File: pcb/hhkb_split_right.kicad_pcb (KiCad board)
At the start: 4 copper layers, 173.7 x 97.4 mm, 84 parts, among them SW1 6, SW10 Y, SW11 U, SW12 I, SW13 O, SW14 P, SW15 [, SW16 ], SW17 Del, SW18 H, SW19 J, SW2 7, SW20 K, SW21 L, SW22 ;, SW23 ', SW24 Enter, SW25 N, SW26 M, SW27 ,, SW28 ., SW29 /, SW3 8, SW30 Shift, SW31 Fn, SW32 R-Space, SW33 Meta, SW34 Alt, SW4 9, SW5 0, SW6 -, SW7 =, SW8 \, SW9 `, U1 74HC595, U2 74HC595

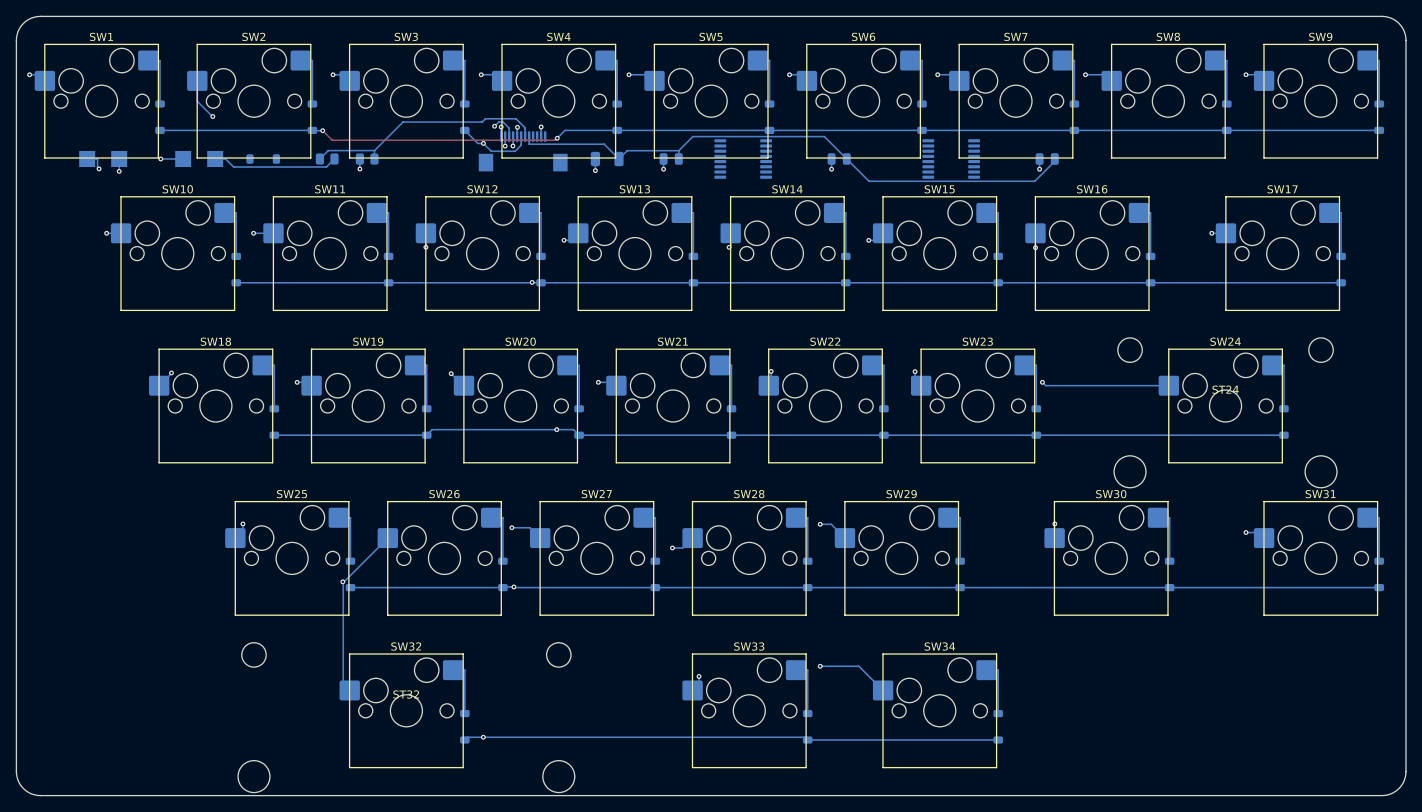
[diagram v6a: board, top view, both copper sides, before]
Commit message: マトリクスのダイオードを SD103AW にした（打ち止めが保証値で決まる）
1N4148W は **1mA 未満の Vf 最大値を規定していない**。行に届くのは
（レール − Vf）で nRF52840 の VIH は 0.7×レール、つまり レール ≧ Vf/0.3。
1mA の最大 0.715V で詰めるとレール 2.55V（1.48V/本）が必要になり、
**打ち止めが 1.12〜1.48V/本 の間で不定だった。電池が減るとキーが
反応しなくなる。**

SD103AW（C130875）は **VF ≦ 0.37V @ 20mA を保証**している。実使用は
100µA でそれよりはるかに小さい。必要なレールは 1.40V で、マイコンの
1.80V の内側。**打ち止めはマイコン律速の 1.10V/本 に戻った。実測不要。**

  逆漏れ 5µA @ 30V（実使用 2V ではさらに小さい）。プルダウン 13kΩ に対し
  誤検出には 20 個以上の同時押しが要る
  フットプリントは同じ SOD-123。**基板は変わらない**（Value は B.Fab のみ）
  単価 $0.0116 で 1N4148W とほぼ同じ。Basic → Extended で +$3

3 基板とも DRC 0 / 未配線 0。検査 292 件。部品 8 種すべて在庫を再確認した。
C4 からダイオードの実測手順を削り、provisional-values から
MATRIX_DIODE_VF を外した（保証値になったため）。

Co-Authored-By: Claude Opus 5 (1M context) <noreply@anthropic.com>
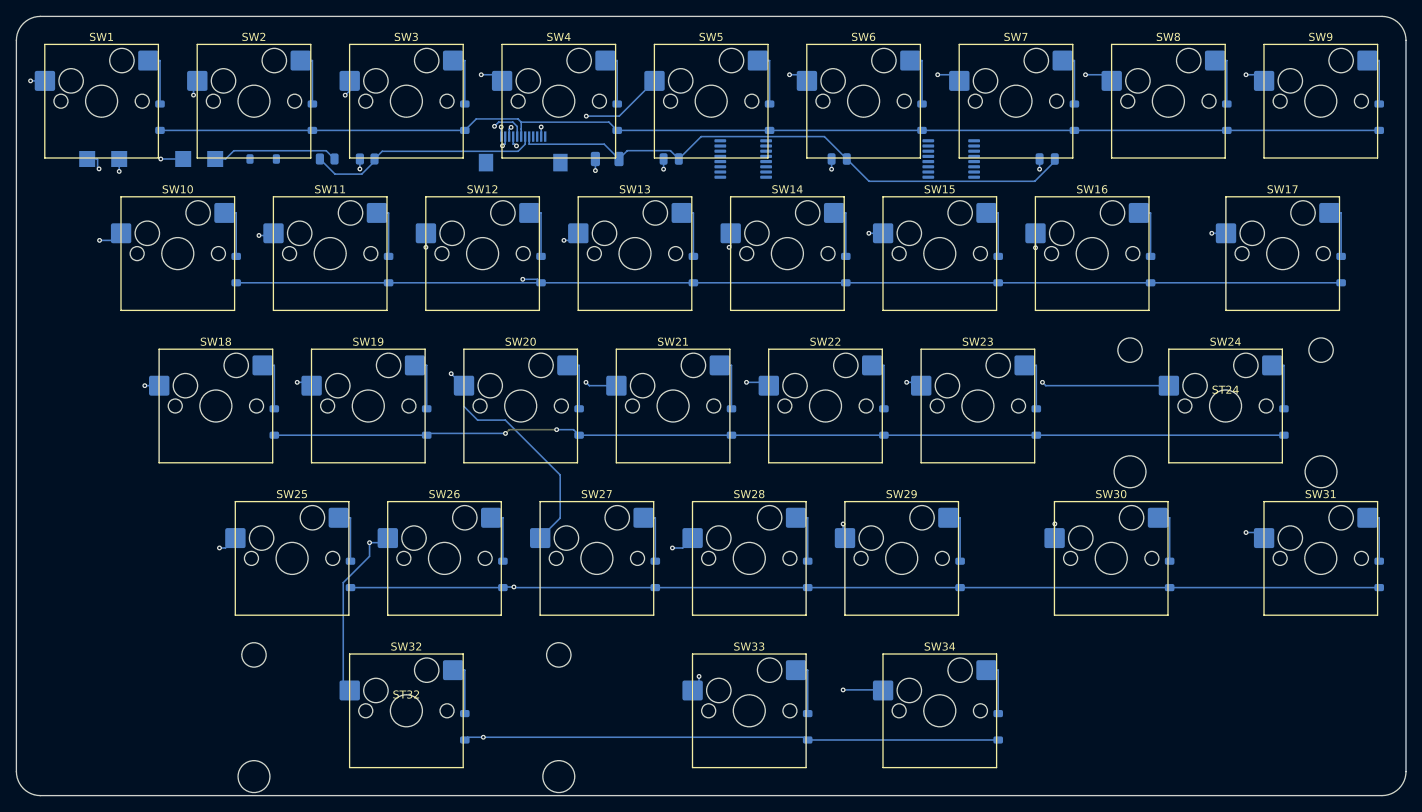
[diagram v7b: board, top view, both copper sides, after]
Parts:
- D1, D10, D11, D12, D13, D14, D15, D16, D17, D18, D19, D2, D20, D21, D22, D23, D24, D25, D26, D27, D28, D29, D3, D30, D31, D32, D33, D34, D4, D5, D6, D7, D8, D9: value 1N4148W -> SD103AW
- U1, U2: value 74HC595 -> 74LVC595
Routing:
- net ROW0: track 163.3 -> 155.4 mm, vias 3 -> 0
- net ROW1: track 160.1 -> 167.1 mm
- net COL2: track 99.1 -> 92.7 mm
- net COL1: track 74.8 -> 78.0 mm
- net VBATT_SENSE: track 30.3 -> 29.1 mm
- net COL4: track 98.8 -> 99.8 mm
- net ROW3: track 194.6 -> 193.7 mm
- net ROW4: track 148.4 -> 149.4 mm
- net COL5: track 101.0 -> 100.1 mm
- net ROW2: track 167.3 -> 166.6 mm, vias 2 -> 3
- net COL3: track 74.9 -> 75.5 mm, vias 4 -> 3
- net COL0: track 27.8 -> 28.4 mm

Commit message: マトリクスのダイオードを 1N4148W へ戻した（SD103AW への変更は誤り）
効く parameter は 2 つあり、片方だけ見て替えたため取り替えっこになっていた。

  (a) 走査電流での Vf … 行に届くのは（レール − Vf）。レール ≧ Vf/0.3
  (b) 逆漏れ … ダイオード本来の役目（ゴースト防止）

  型番      (a) Vf の保証         (b) 逆漏れの保証    単価/305個
  1N4148W   なし(1mA で 0.715V)   25nA @ 20V          $3.57 Basic ← 採用
  SD103AW   0.37V @ 20mA          なし(30V で 5µA)    $3.54 +$3
  BAT46W    250mV @ 0.1mA         0.5µA @ 1.5V        $28.1 +$3

SD103AW は逆漏れの保証が動作点に無い。30V の 5µA を当てると、
プルダウン 13kΩ に対して **2 個同時押しでもゴーストの margin を割る**
（引き下げ 130mV に対し余裕 120mV）。**誤った文字が出る側の失敗**なので、
打ち止めが不定であることより害が大きい。

1N4148W は逆漏れが桁違いに小さく本来の役目は保証される。不定なのは
打ち止めだけで、これは「電池が早く終わる」であって誤動作ではない。

BAT46W は両方を動作点で保証する唯一の候補（VF ≦ 250mV @ 0.1mA、
IR ≦ 0.5µA @ 1.5V）。**+$24.5（¥3,700）。**実測が難しければここへ戻る。

C4 の測定手順を戻した。**1N4007 では測れない**ことを明記した（接合が
大きく Vf が低く出る）。1N4148 が無ければ測定は飛ばしてよい。

3 基板とも DRC 0 / 未配線 0。検査 292 件。

Co-Authored-By: Claude Opus 5 (1M context) <noreply@anthropic.com>
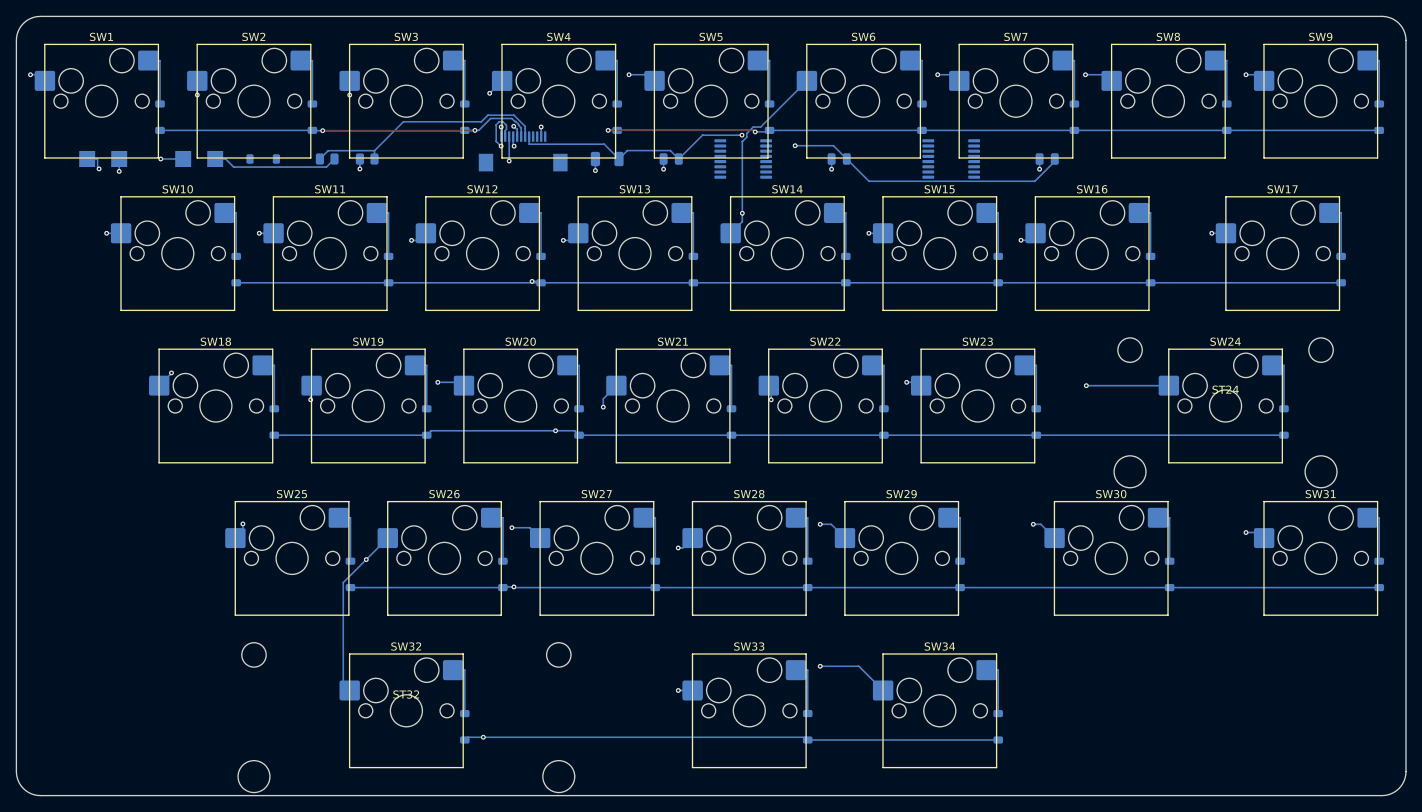
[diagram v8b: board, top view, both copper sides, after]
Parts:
- D1, D10, D11, D12, D13, D14, D15, D16, D17, D18, D19, D2, D20, D21, D22, D23, D24, D25, D26, D27, D28, D29, D3, D30, D31, D32, D33, D34, D4, D5, D6, D7, D8, D9: value SD103AW -> 1N4148W
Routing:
- net ROW0: track 155.4 -> 164.0 mm, vias 0 -> 4
- net ROW4: track 149.4 -> 154.4 mm
- net ROW3: track 193.7 -> 189.4 mm
- net COL1: track 78.0 -> 74.2 mm
- net ROW1: track 167.1 -> 164.1 mm
- net COL2: track 92.7 -> 90.1 mm
- net COL7: track 82.9 -> 85.5 mm
- net VBATT_SENSE: track 29.1 -> 30.8 mm
- net COL0: track 28.4 -> 27.7 mm
- net COL5: track 100.1 -> 99.8 mm, vias 5 -> 4
- net V3V3: track 73.1 -> 73.2 mm, vias 0 -> 2
- net ROW2: track 166.6 -> 166.5 mm, vias 3 -> 2
- net COL3: track 75.5 -> 75.4 mm, vias 3 -> 4
